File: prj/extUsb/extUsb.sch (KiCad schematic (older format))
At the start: 22 parts, among them J1 USB_B_Micro, J2 Conn_01x05, U1 SN74LVC2T45, U2 MIC5504-3.3YM5, U3 TS5A3166DBVR

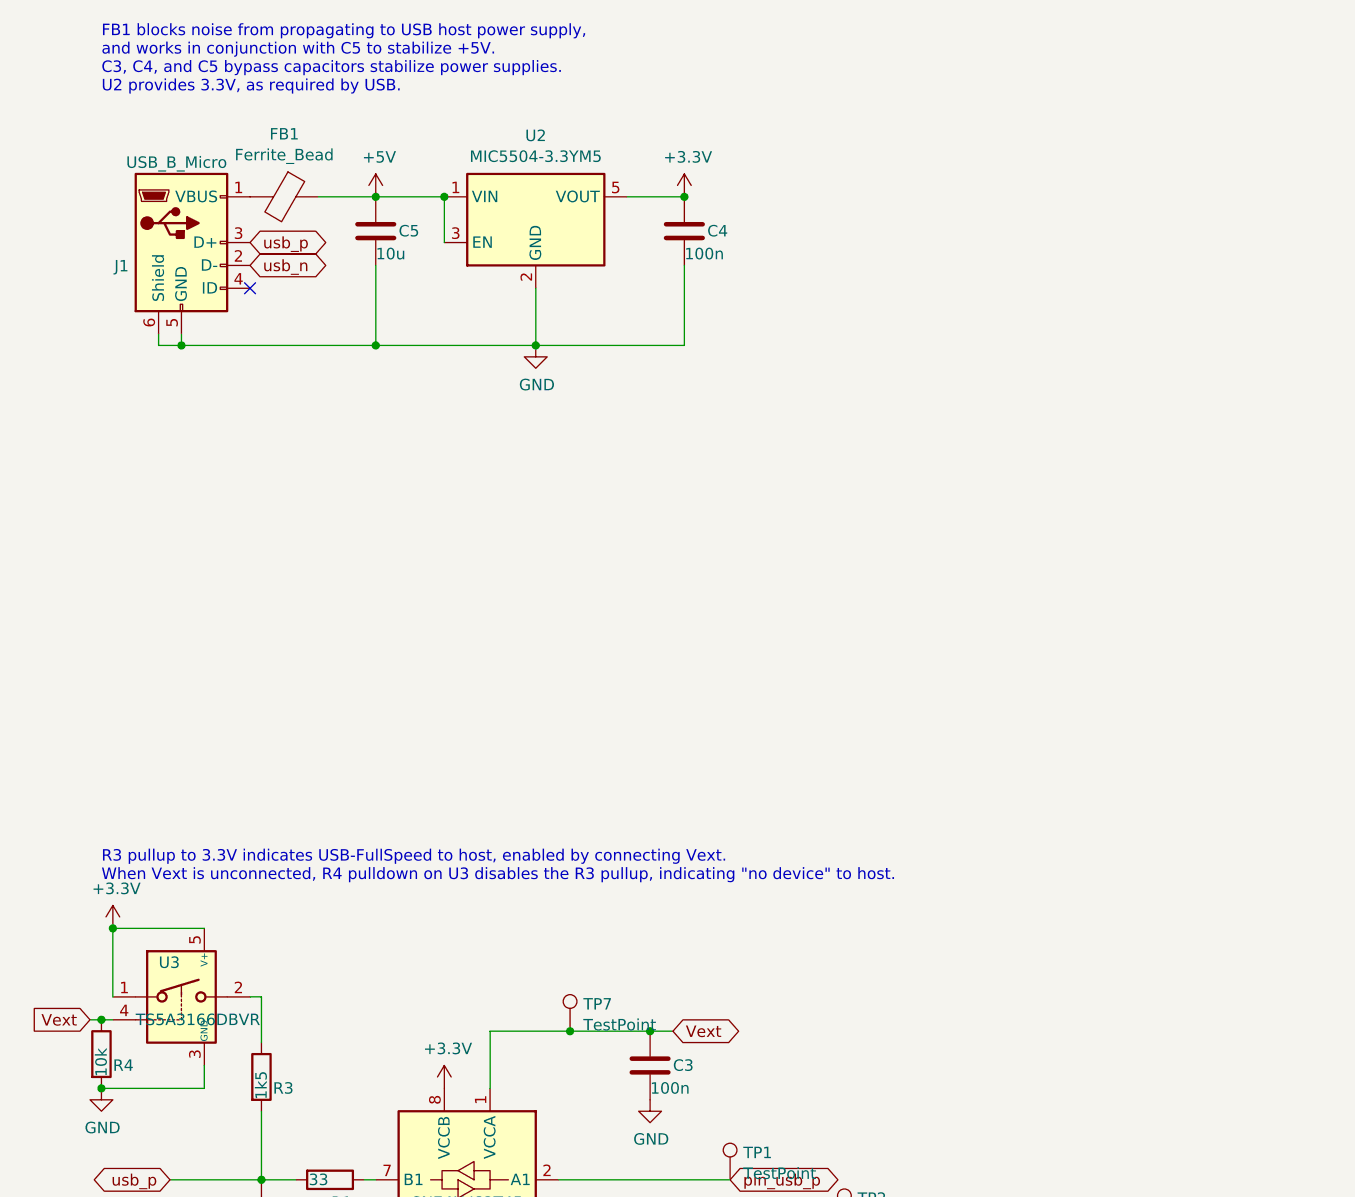
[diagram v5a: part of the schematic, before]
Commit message: extUsb Schematic passing DRC and release for analog switch.
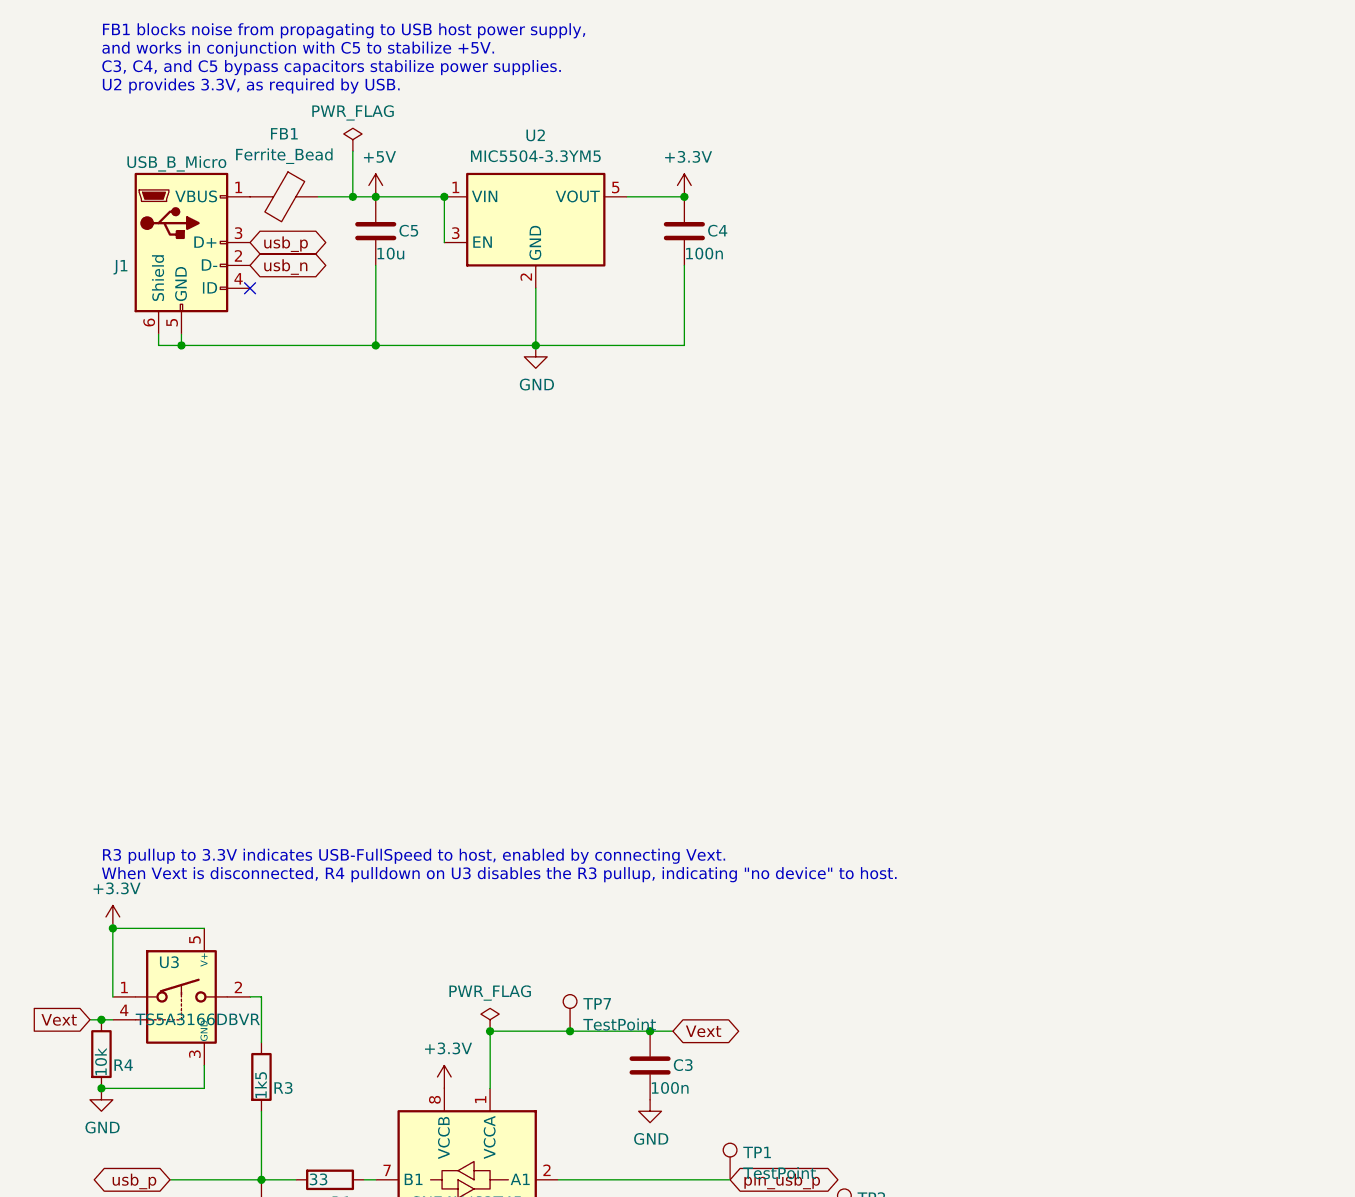
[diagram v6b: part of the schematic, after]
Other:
- note added: "R3 pullup to 3.3V indicates USB-FullSpeed to host, enabled by connecting Vext.\nWhen Vext is disconnected, R4 pulldown on U3 disables the R3 pullup, indicating "no device" to host."
- note removed: "R3 pullup to 3.3V indicates USB-FullSpeed to host, enabled by connecting Vext.\nWhen Vext is unconnected, R4 pulldown on U3 disables the R3 pullup, indicating "no device" to host."
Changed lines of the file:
@@
 	1    0    0    -1
 $EndComp
-Wire Wire Line
-	2700 5450 2700 5700
 $Comp
 L Device:C C1
@@
 Wire Wire Line
 	1700 6700 1850 6700
-$Comp
-L Logic_LevelTranslator:SN74LVC2T45DCUR U1
-U 1 1 5F998087
-P 2600 6200
-F 0 "U1" H 2800 5850 50  0000 C CNN
-F 1 "SN74LVC2T45" H 2600 6200 50  0000 C CNN
-F 2 "Package_SO:SSOP-8_2.95x2.8mm_P0.65mm" H 2650 5650 50  0001 C CNN
-F 3 "http://www.ti.com/lit/ds/symlink/sn74lvc2t45.pdf" H 1700 5650 50  0001 C CNN
-	1    2600 6200
-	-1   0    0    -1
-$EndComp
 $Comp
 L Device:Ferrite_Bead FB1
@@
 $EndComp
 Wire Wire Line
-	1950 1800 2200 1800
+	1950 1800 2100 1800
 $Comp
 L Device:R R4
@@
 Wire Wire Line
 	1000 5400 1050 5400
-Text Notes 1000 4800 0    50   ~ 0
-R3 pullup to 3.3V indicates USB-FullSpeed to host, enabled by connecting Vext.\nWhen Vext is unconnected, R4 pulldown on U3 disables the R3 pullup, indicating "no device" to host.
 Text Notes 1000 7450 0    50   ~ 0
 R1 and R2 series termination protect D+,D- transmission lines against device-to-host transient voltage spikes.\nOptionally (with C1,C2) include low-pass filtering.
@@
 Connection ~ 1000 5700
 Wire Wire Line
+	1650 5300 1700 5300
+Wire Wire Line
+	3400 5450 3050 5450
+Wire Wire Line
+	3300 1800 3550 1800
+Wire Wire Line
+	2200 1800 2500 1800
+$Comp
+L Connector:TestPoint TP2
+U 1 1 5FA881AA
+P 4250 6300
+F 0 "TP2" H 4308 6418 50  0000 L CNN
+F 1 "TestPoint" H 4308 6327 50  0000 L CNN
+F 2 "TestPoint:TestPoint_Pad_D2.0mm" H 4450 6300 50  0001 C CNN
+F 3 "~" H 4450 6300 50  0001 C CNN
+	1    4250 6300
+	1    0    0    -1
+$EndComp
+$Comp
+L Connector:TestPoint TP1
+U 1 1 5FA87D46
+P 3750 6100
+F 0 "TP1" H 3808 6218 50  0000 L CNN
+F 1 "TestPoint" H 3808 6127 50  0000 L CNN
+F 2 "" H 3950 6100 50  0001 C CNN
+F 3 "~" H 3950 6100 50  0001 C CNN
+	1    3750 6100
+	1    0    0    -1
+$EndComp
+Wire Wire Line
+	1300 6700 1700 6700
+Wire Wire Line
+	1300 6100 1700 6100
+$Comp
+L Connector:TestPoint TP4
+U 1 1 5FAA3783
+P 10100 3900
+F 0 "TP4" H 10158 4018 50  0000 L CNN
+F 1 "TestPoint" H 10158 3927 50  0000 L CNN
+F 2 "TestPoint:TestPoint_Pad_D2.0mm" H 10300 3900 50  0001 C CNN
+F 3 "~" H 10300 3900 50  0001 C CNN
+	1    10100 3900
+	1    0    0    -1
+$EndComp
+$Comp
+L Connector:TestPoint TP5
+U 1 1 5FAA3DCC
+P 10100 4150
+F 0 "TP5" H 10158 4268 50  0000 L CNN
+F 1 "TestPoint" H 10158 4177 50  0000 L CNN
+F 2 "TestPoint:TestPoint_Pad_D2.0mm" H 10300 4150 50  0001 C CNN
+F 3 "~" H 10300 4150 50  0001 C CNN
+	1    10100 4150
+	1    0    0    -1
+$EndComp
+$Comp
+L Connector:TestPoint TP6
+U 1 1 5FAA4E02
+P 10100 4400
+F 0 "TP6" H 10158 4518 50  0000 L CNN
+F 1 "TestPoint" H 10158 4427 50  0000 L CNN
+F 2 "TestPoint:TestPoint_Pad_D2.0mm" H 10300 4400 50  0001 C CNN
+F 3 "~" H 10300 4400 50  0001 C CNN
+	1    10100 4400
+	1    0    0    -1
+$EndComp
+$Comp
+L Connector:TestPoint TP3
+U 1 1 5FAA52CF
+P 3750 6500
+F 0 "TP3" H 3808 6618 50  0000 L CNN
+F 1 "TestPoint" H 3808 6527 50  0000 L CNN
+F 2 "TestPoint:TestPoint_Pad_D2.0mm" H 3950 6500 50  0001 C CNN
+F 3 "~" H 3950 6500 50  0001 C CNN
+	1    3750 6500
+	1    0    0    -1
+$EndComp
+Wire Wire Line
+	3000 6500 3750 6500
+$Comp
+L power:GND #PWR0104
+U 1 1 5FAA8E6F
+P 10000 4400
+F 0 "#PWR0104" H 10000 4150 50  0001 C CNN
+F 1 "GND" H 10005 4227 50  0000 C CNN
+F 2 "" H 10000 4400 50  0001 C CNN
+F 3 "" H 10000 4400 50  0001 C CNN
+	1    10000 4400
+	1    0    0    -1
+$EndComp
+Wire Wire Line
+	10000 4400 10100 4400
+Wire Wire Line
+	10000 4400 10000 4150
+Wire Wire Line
+	10000 3900 10100 3900
+Connection ~ 10000 4400
+Wire Wire Line
+	10100 4150 10000 4150
+Connection ~ 10000 4150
+Wire Wire Line
+	10000 4150 10000 3900
+$Comp
+L Connector:TestPoint TP7
+U 1 1 5FAB2342
+P 3050 5450
+F 0 "TP7" H 3108 5568 50  0000 L CNN
+F 1 "TestPoint" H 3108 5477 50  0000 L CNN
+F 2 "TestPoint:TestPoint_Pad_D2.0mm" H 3250 5450 50  0001 C CNN
+F 3 "~" H 3250 5450 50  0001 C CNN
+	1    3050 5450
+	1    0    0    -1
+$EndComp
+Connection ~ 3050 5450
+Wire Wire Line
+	3000 6100 3750 6100
+Wire Wire Line
+	3000 6300 4250 6300
+$Comp
+L Logic_LevelTranslator:SN74LVC2T45DCUR U1
+U 1 1 5F998087
+P 2600 6200
+F 0 "U1" H 2800 5850 50  0000 C CNN
+F 1 "SN74LVC2T45" H 2600 6200 50  0000 C CNN
+F 2 "Package_SO:SSOP-8_2.95x2.8mm_P0.65mm" H 2650 5650 50  0001 C CNN
+F 3 "http://www.ti.com/lit/ds/symlink/sn74lvc2t45.pdf" H 1700 5650 50  0001 C CNN
+	1    2600 6200
+	-1   0    0    -1
+$EndComp
+Wire Wire Line
+	1700 5300 1700 5500
+Text Notes 1000 4800 0    50   ~ 0
+R3 pullup to 3.3V indicates USB-FullSpeed to host, enabled by connecting Vext.\nWhen Vext is disconnected, R4 pulldown on U3 disables the R3 pullup, indicating "no device" to host.
+Connection ~ 1050 5000
+Wire Wire Line
 	1050 5300 1050 5000
 Wire Wire Line
 	1050 5000 1450 5000
-Connection ~ 1050 5000
-Wire Wire Line
-	1650 5300 1700 5300
-Wire Wire Line
-	1700 5300 1700 5500
 $Comp
 L Analog_Switch:TS5A3166DBVR U3
@@
 $EndComp
 Wire Wire Line
-	3400 5450 3050 5450
-Wire Wire Line
-	3300 1800 3550 1800
-Wire Wire Line
-	2200 1800 2500 1800
-$Comp
-L Connector:TestPoint TP2
-U 1 1 5FA881AA
-P 4250 6300
-F 0 "TP2" H 4308 6418 50  0000 L CNN
-F 1 "TestPoint" H 4308 6327 50  0000 L CNN
-F 2 "TestPoint:TestPoint_Pad_D2.0mm" H 4450 6300 50  0001 C CNN
-F 3 "~" H 4450 6300 50  0001 C CNN
-	1    4250 6300
-	1    0    0    -1
-$EndComp
-$Comp
-L Connector:TestPoint TP1
-U 1 1 5FA87D46
-P 3750 6100
-F 0 "TP1" H 3808 6218 50  0000 L CNN
-F 1 "TestPoint" H 3808 6127 50  0000 L CNN
-F 2 "" H 3950 6100 50  0001 C CNN
-F 3 "~" H 3950 6100 50  0001 C CNN
-	1    3750 6100
-	1    0    0    -1
-$EndComp
-Wire Wire Line
-	3000 6100 3750 6100
-Wire Wire Line
-	1300 6700 1700 6700
-Wire Wire Line
-	1300 6100 1700 6100
-Wire Wire Line
-	3000 6300 4250 6300
-$Comp
-L Connector:TestPoint TP4
-U 1 1 5FAA3783
-P 10100 3900
-F 0 "TP4" H 10158 4018 50  0000 L CNN
-F 1 "TestPoint" H 10158 3927 50  0000 L CNN
-F 2 "TestPoint:TestPoint_Pad_D2.0mm" H 10300 3900 50  0001 C CNN
-F 3 "~" H 10300 3900 50  0001 C CNN
-	1    10100 3900
-	1    0    0    -1
-$EndComp
-$Comp
-L Connector:TestPoint TP5
-U 1 1 5FAA3DCC
-P 10100 4150
-F 0 "TP5" H 10158 4268 50  0000 L CNN
-F 1 "TestPoint" H 10158 4177 50  0000 L CNN
-F 2 "TestPoint:TestPoint_Pad_D2.0mm" H 10300 4150 50  0001 C CNN
-F 3 "~" H 10300 4150 50  0001 C CNN
-	1    10100 4150
-	1    0    0    -1
-$EndComp
-$Comp
-L Connector:TestPoint TP6
-U 1 1 5FAA4E02
-P 10100 4400
-F 0 "TP6" H 10158 4518 50  0000 L CNN
-F 1 "TestPoint" H 10158 4427 50  0000 L CNN
-F 2 "TestPoint:TestPoint_Pad_D2.0mm" H 10300 4400 50  0001 C CNN
-F 3 "~" H 10300 4400 50  0001 C CNN
-	1    10100 4400
-	1    0    0    -1
-$EndComp
-$Comp
-L Connector:TestPoint TP3
-U 1 1 5FAA52CF
-P 3750 6500
-F 0 "TP3" H 3808 6618 50  0000 L CNN
-F 1 "TestPoint" H 3808 6527 50  0000 L CNN
-F 2 "TestPoint:TestPoint_Pad_D2.0mm" H 3950 6500 50  0001 C CNN
-F 3 "~" H 3950 6500 50  0001 C CNN
-	1    3750 6500
-	1    0    0    -1
-$EndComp
-Wire Wire Line
-	3000 6500 3750 6500
-$Comp
-L power:GND #PWR0104
-U 1 1 5FAA8E6F
-P 10000 4400
-F 0 "#PWR0104" H 10000 4150 50  0001 C CNN
-F 1 "GND" H 10005 4227 50  0000 C CNN
-F 2 "" H 10000 4400 50  0001 C CNN
-F 3 "" H 10000 4400 50  0001 C CNN
-	1    10000 4400
-	1    0    0    -1
-$EndComp
-Wire Wire Line
-	10000 4400 10100 4400
-Wire Wire Line
-	10000 4400 10000 4150
-Wire Wire Line
-	10000 3900 10100 3900
-Connection ~ 10000 4400
-Wire Wire Line
-	10100 4150 10000 4150
-Connection ~ 10000 4150
-Wire Wire Line
-	10000 4150 10000 3900
-$Comp
-L Connector:TestPoint TP7
-U 1 1 5FAB2342
-P 3050 5450
-F 0 "TP7" H 3108 5568 50  0000 L CNN
-F 1 "TestPoint" H 3108 5477 50  0000 L CNN
-F 2 "TestPoint:TestPoint_Pad_D2.0mm" H 3250 5450 50  0001 C CNN
-F 3 "~" H 3250 5450 50  0001 C CNN
-	1    3050 5450
-	1    0    0    -1
-$EndComp
-Connection ~ 3050 5450
+	2700 5450 2700 5700
 Wire Wire Line
 	3050 5450 2700 5450
+$Comp
+L power:PWR_FLAG #FLG0101
+U 1 1 5FA98ACB
+P 2100 1600
+F 0 "#FLG0101" H 2100 1675 50  0001 C CNN
+F 1 "PWR_FLAG" H 2100 1773 50  0000 C CNN
+F 2 "" H 2100 1600 50  0001 C CNN
+F 3 "~" H 2100 1600 50  0001 C CNN
+	1    2100 1600
+	1    0    0    -1
+$EndComp
+Wire Wire Line
+	2100 1600 2100 1800
+Connection ~ 2100 1800
+Wire Wire Line
+	2100 1800 2200 1800
+$Comp
+L power:PWR_FLAG #FLG0102
+U 1 1 5FA9C183
+P 2700 5450
+F 0 "#FLG0102" H 2700 5525 50  0001 C CNN
+F 1 "PWR_FLAG" H 2700 5623 50  0000 C CNN
+F 2 "" H 2700 5450 50  0001 C CNN
+F 3 "~" H 2700 5450 50  0001 C CNN
+	1    2700 5450
+	1    0    0    -1
+$EndComp
+Connection ~ 2700 5450
 $EndSCHEMATC

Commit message: extUsb version3 without short on body of USB connector.
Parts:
- removed C1, C2: 18p, Capacitor_SMD:C_0603_1608Metric_Pad1.08x0.95mm_HandSolder, symbol Device:C
- J1: symbol Connector:USB_B_Micro -> extUsb-rescue:USB_B_Micro-Connector
- U1: symbol Logic_LevelTranslator:SN74LVC2T45DCUR -> extUsb-rescue:SN74LVC2T45DCUR-Logic_LevelTranslator
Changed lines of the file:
@@
 EESchema Schematic File Version 4
-EELAYER 30 0
+LIBS:extUsb-cache
+EELAYER 26 0
 EELAYER END
 $Descr A4 11693 8268
@@
 $EndComp
 $Comp
-L Connector:USB_B_Micro J1
+L extUsb-rescue:USB_B_Micro-Connector J1
 U 1 1 5F998976
 P 1350 2000
@@
 	1    0    0    -1
 $EndComp
-$Comp
-L Device:C C1
-U 1 1 5FA1C049
-P 1700 6250
-F 0 "C1" H 1800 6250 50  0000 L CNN
-F 1 "18p" H 1700 6150 50  0000 L CNN
-F 2 "Capacitor_SMD:C_0603_1608Metric_Pad1.08x0.95mm_HandSolder" H 1738 6100 50  0001 C CNN
-F 3 "~" H 1700 6250 50  0001 C CNN
-	1    1700 6250
-	1    0    0    -1
-$EndComp
-$Comp
-L Device:C C2
-U 1 1 5FA1CC20
-P 1700 6850
-F 0 "C2" H 1800 6850 50  0000 L CNN
-F 1 "18p" H 1700 6750 50  0000 L CNN
-F 2 "Capacitor_SMD:C_0603_1608Metric_Pad1.08x0.95mm_HandSolder" H 1738 6700 50  0001 C CNN
-F 3 "~" H 1700 6850 50  0001 C CNN
-	1    1700 6850
-	1    0    0    -1
-$EndComp
-$Comp
-L power:GND #PWR0101
-U 1 1 5FA1D04B
-P 1700 7000
-F 0 "#PWR0101" H 1700 6750 50  0001 C CNN
-F 1 "GND" H 1705 6827 50  0000 C CNN
-F 2 "" H 1700 7000 50  0001 C CNN
-F 3 "" H 1700 7000 50  0001 C CNN
-	1    1700 7000
-	1    0    0    -1
-$EndComp
-$Comp
-L power:GND #PWR0102
-U 1 1 5FA1ECAC
-P 1700 6400
-F 0 "#PWR0102" H 1700 6150 50  0001 C CNN
-F 1 "GND" H 1705 6227 50  0000 C CNN
-F 2 "" H 1700 6400 50  0001 C CNN
-F 3 "" H 1700 6400 50  0001 C CNN
-	1    1700 6400
-	1    0    0    -1
-$EndComp
 Wire Wire Line
 	3500 5450 3400 5450
@@
 	2200 6700 2200 6300
 Connection ~ 1700 6100
-Connection ~ 1700 6700
-Wire Wire Line
-	1700 6700 1850 6700
 $Comp
 L Device:Ferrite_Bead FB1
@@
 $EndComp
 Wire Wire Line
-	1300 6700 1700 6700
-Wire Wire Line
 	1300 6100 1700 6100
 $Comp
@@
 	3000 6300 4250 6300
 $Comp
-L Logic_LevelTranslator:SN74LVC2T45DCUR U1
+L extUsb-rescue:SN74LVC2T45DCUR-Logic_LevelTranslator U1
 U 1 1 5F998087
 P 2600 6200
@@
 $EndComp
 Connection ~ 2700 5450
+Wire Wire Line
+	1300 6700 1850 6700
 $EndSCHEMATC

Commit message: extUsb Final release suitable for laser-etch or commercial fabs.
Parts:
- J1: symbol extUsb-rescue:USB_B_Micro-Connector -> extUsb-cache:USB_B_Micro-Connector
- U1: symbol extUsb-rescue:SN74LVC2T45DCUR-Logic_LevelTranslator -> extUsb-cache:SN74LVC2T45DCUR-Logic_LevelTranslator
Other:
- note added: "R1 and R2 series termination protect D+,D- transmission lines against device-to-host transient voltage spikes."
- note removed: "R1 and R2 series termination protect D+,D- transmission lines against device-to-host transient voltage spikes.\nOptionally (with C1,C2) include low-pass filtering."
- moved on the sheet: R2
